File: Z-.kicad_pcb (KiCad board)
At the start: 4 copper layers, 98 x 98 mm, 147 parts, among them J1 200528-0100, J2 U.FL, J3 U.FL, J5 Conn_01x02, Q1 NX3008NBKS, Q10 MBT2222ADW1T1, Q11 NX3008NBKS, Q12 MBT2222ADW1T1, Q13 IRLML2803, Q14 SiRA99DP, Q15 IRFTS9342PBF, Q17 IRFTS9342PBF, Q19 IRFTS9342PBF, Q2 MBT2222ADW1T1, Q20 IRLML2803, Q21 SiRA99DP, Q3 NX3008NBKS, Q4 MBT2222ADW1T1, Q5 NX3008NBKS, Q6 MBT2222ADW1T1, Q7 NX3008NBKS, Q8 MBT2222ADW1T1, Q9 NX3008NBKS, U1 OPT4003DNPRQ1, U2 PCA9633DP2, U4 DRV8235RTER, U5 USBLC6-2P6

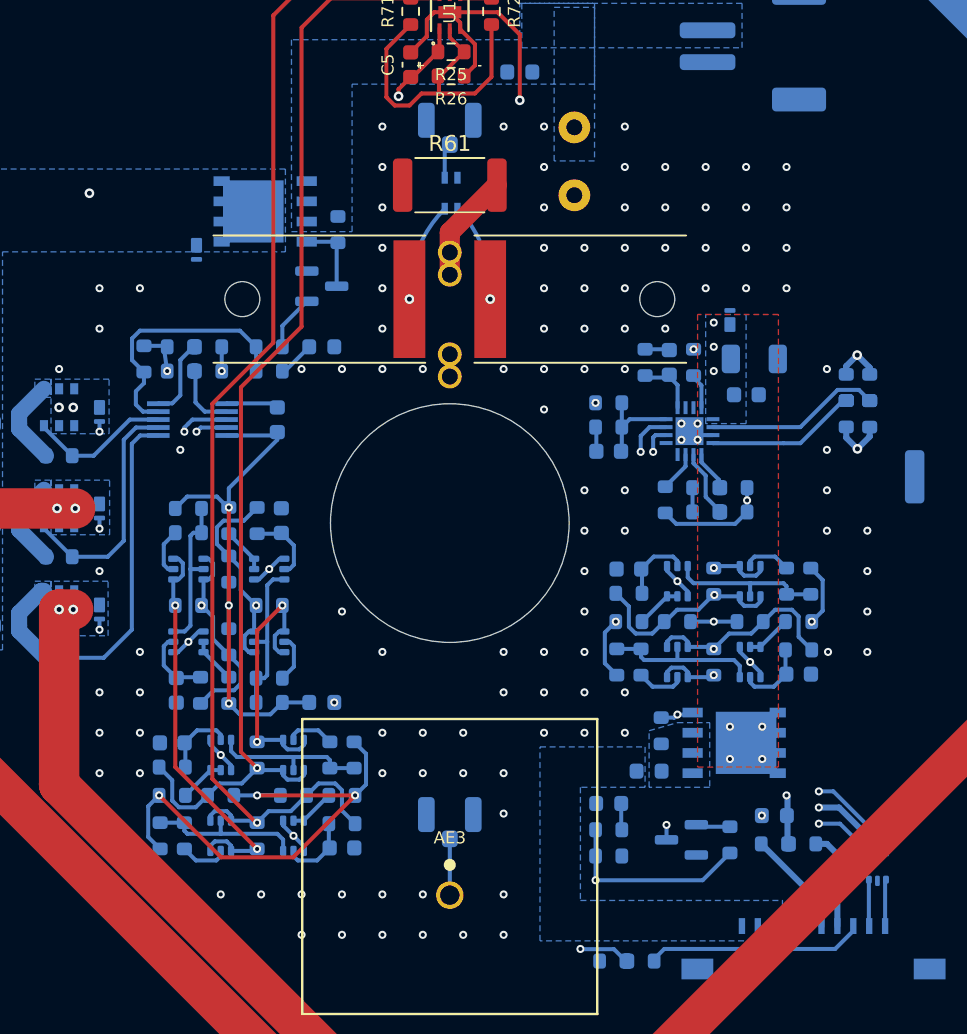
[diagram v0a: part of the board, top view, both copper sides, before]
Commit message: Started adding pmos -> relay
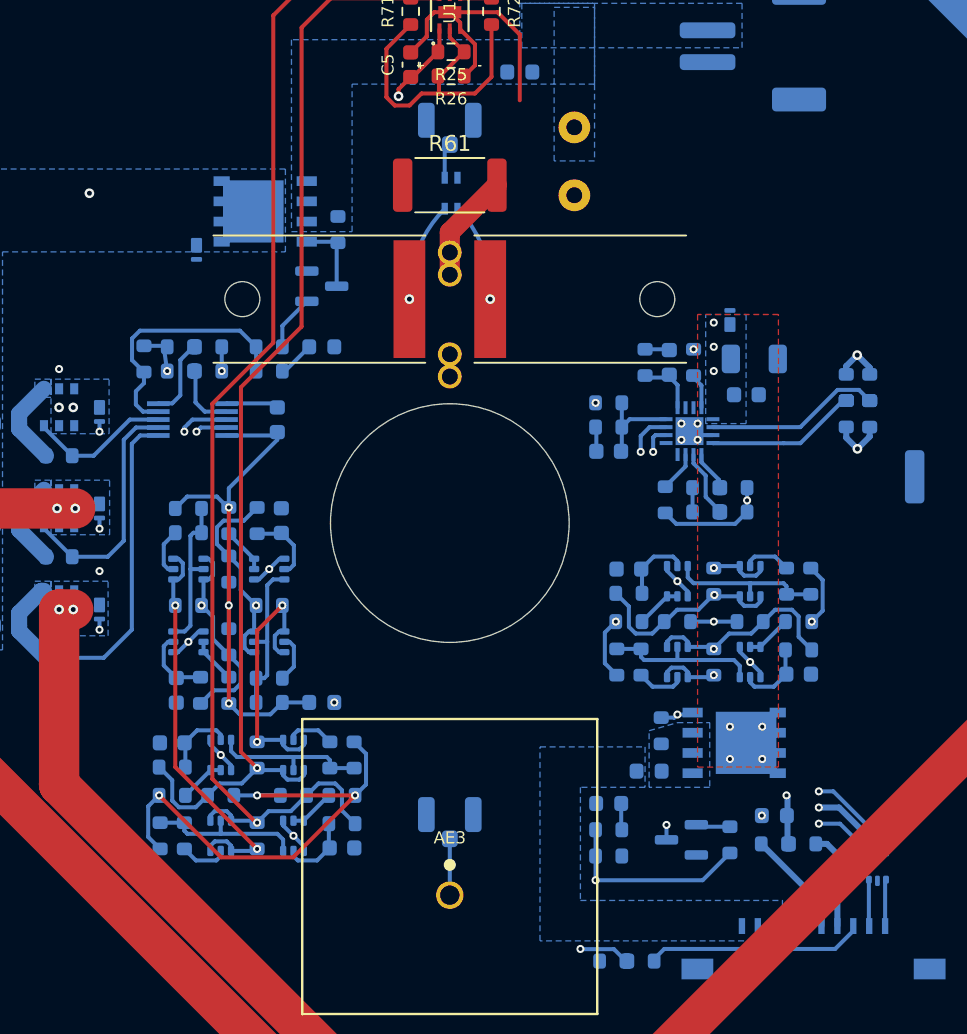
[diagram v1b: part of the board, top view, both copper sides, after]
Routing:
- net GND: vias 128 -> 21
